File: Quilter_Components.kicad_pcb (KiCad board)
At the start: 4 copper layers, 40.4 x 100 mm, 160 parts, among them J1 Conn_01x10_Male, J2 Conn_01x10_Male, J3 Conn_01x10_Male, J4 Eurorack_10_pin_power, U1 TL072, U10 SSI2144, U2 TL074, U3 TL074, U4 TL074, U5 SSI2144, U7 SSI2144, U9 SSI2144

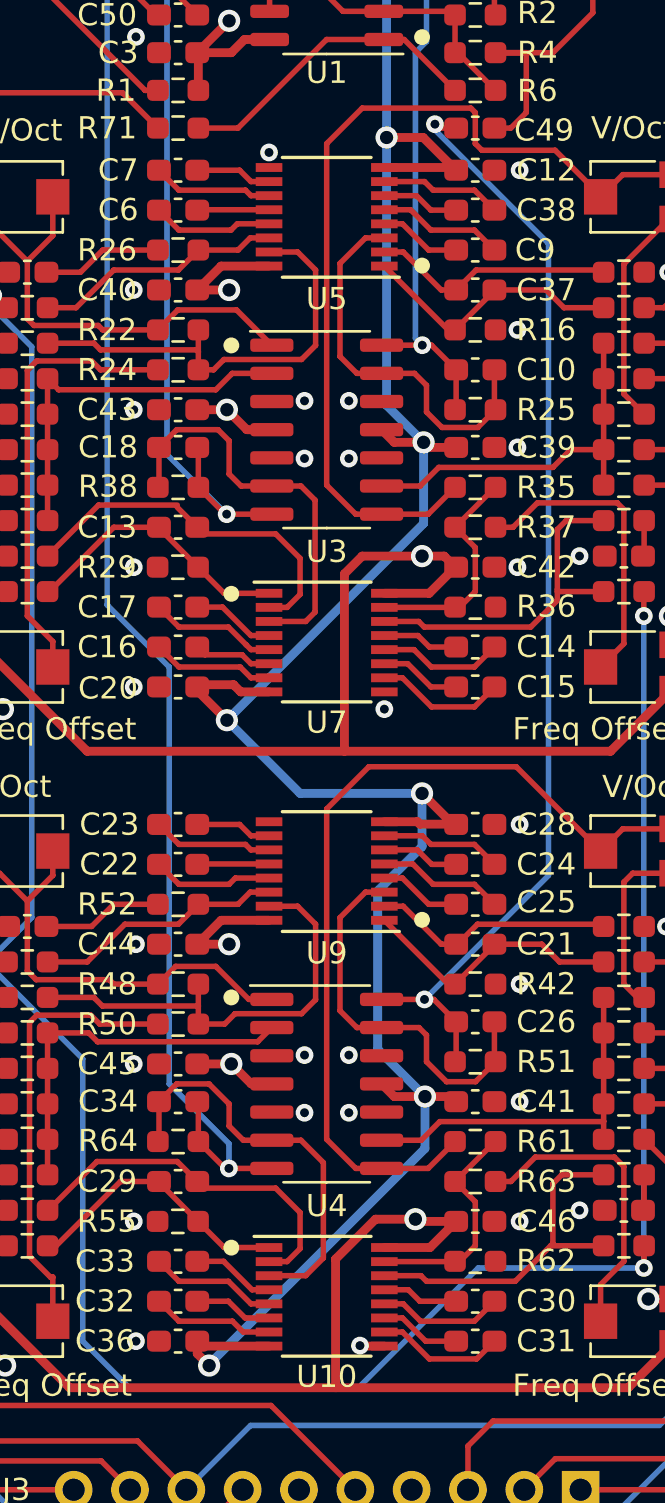
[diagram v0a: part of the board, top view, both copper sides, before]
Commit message: Reorganised components gerber location
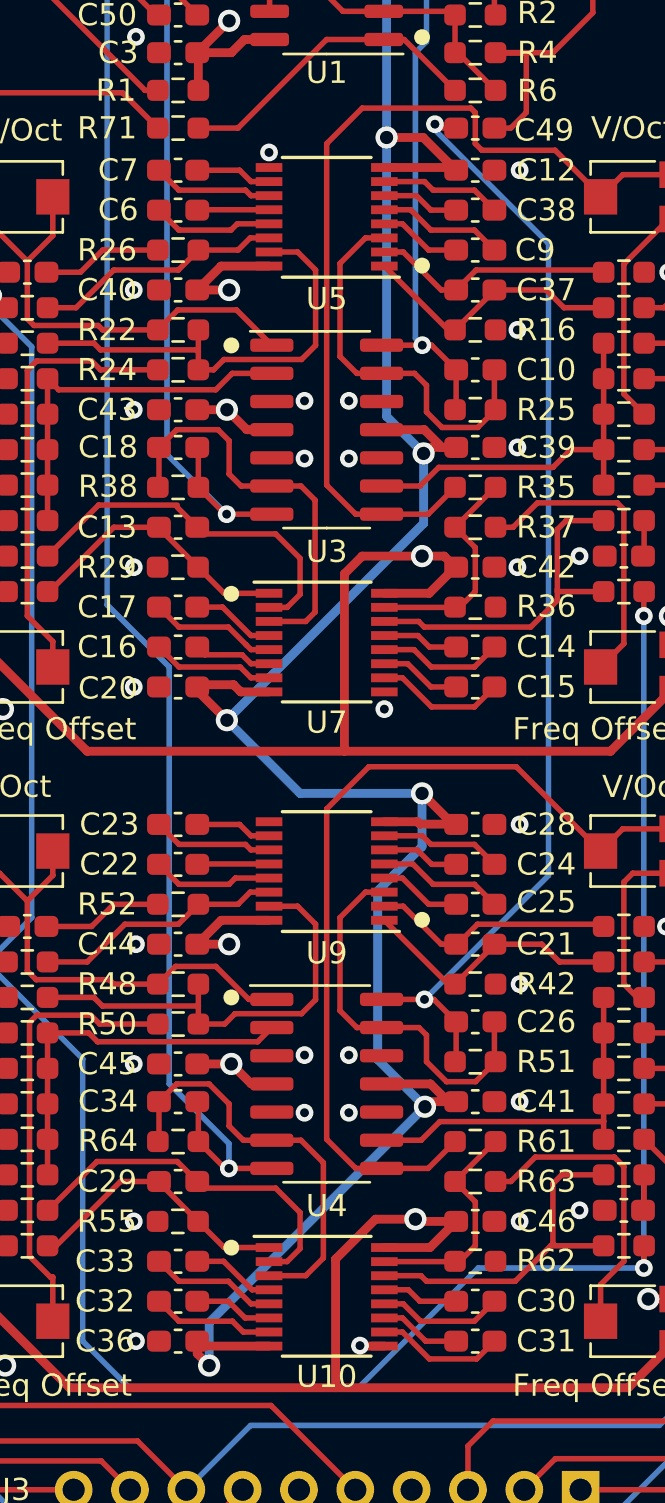
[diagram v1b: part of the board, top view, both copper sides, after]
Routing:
- net -12V: track 226.2 -> 228.5 mm
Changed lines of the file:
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@@
     (pad_to_mask_clearance 0)
     (pcbplotparams
-      (layerselection 0x00010fc_ffffffff)
+      (layerselection 0x00010f0_ffffffff)
       (disableapertmacros false)
       (usegerberextensions false)
@@
       (drillshape 0)
       (scaleselection 1)
-      (outputdirectory "Gerbers/Components/")
+      (outputdirectory "Gerbers/Quilter_Components/")
     )
   )
@@
   (segment (start 64.3625 141.7625) (end 64.9 142.3) (width 0.4) (layer "F.Cu") (net 3))
   (segment (start 66 111.6) (end 64.4625 111.6) (width 0.4) (layer "F.Cu") (net 3))
-  (segment (start 74.57 100.67) (end 73.245 100.67) (width 0.4) (layer "F.Cu") (net 3))
+  (segment (start 74.84 100.9) (end 74.57 101.17) (width 0.4) (layer "F.Cu") (net 3))
   (segment (start 65.2625 70.4) (end 64.3625 69.5) (width 0.4) (layer "F.Cu") (net 3))
   (segment (start 72.775 78.695) (end 72.78 78.7) (width 0.4) (layer "F.Cu") (net 3))
   (segment (start 67.6 111.9225) (end 66.3225 111.9225) (width 0.4) (layer "F.Cu") (net 3))
-  (segment (start 73.245 130.17) (end 72.675 129.6) (width 0.4) (layer "F.Cu") (net 3))
   (segment (start 51.8 56.1) (end 54.3 53.6) (width 0.4) (layer "F.Cu") (net 3))
   (segment (start 64.4125 62.7) (end 63.0125 61.3) (width 0.4) (layer "F.Cu") (net 3))
-  (segment (start 74.8 100.9) (end 74.57 100.67) (width 0.4) (layer "F.Cu") (net 3))
+  (segment (start 75.4 100.9) (end 74.84 100.9) (width 0.4) (layer "F.Cu") (net 3))
   (segment (start 76.0375 88.4) (end 75.915 88.2775) (width 0.4) (layer "F.Cu") (net 3))
   (segment (start 76.0375 117.9) (end 75.9 117.9) (width 0.4) (layer "F.Cu") (net 3))
+  (segment (start 72.675 129.6) (end 74.881374 129.6) (width 0.4) (layer "F.Cu") (net 3))
   (segment (start 72.8 117.7775) (end 74.29 117.7775) (width 0.4) (layer "F.Cu") (net 3))
-  (segment (start 74.63 130.17) (end 73.245 130.17) (width 0.4) (layer "F.Cu") (net 3))
   (segment (start 74.4375 76.4) (end 72.9 76.4) (width 0.4) (layer "F.Cu") (net 3))
   (segment (start 76.0375 88.4) (end 76.026023 88.4) (width 0.4) (layer "F.Cu") (net 3))
+  (segment (start 72.675 100.1) (end 74.6 100.1) (width 0.4) (layer "F.Cu") (net 3))
   (segment (start 58 61.3) (end 56.8 62.5) (width 0.4) (layer "F.Cu") (net 3))
   (segment (start 54.6 111.8) (end 55.5 112.7) (width 0.4) (layer "F.Cu") (net 3))
   (segment (start 85.8 108.6245) (end 85.6755 108.5) (width 0.4) (layer "F.Cu") (net 3))
+  (segment (start 76.0375 130.4) (end 74.86 130.4) (width 0.4) (layer "F.Cu") (net 3))
   (segment (start 74.29 117.7775) (end 74.4 117.8875) (width 0.4) (layer "F.Cu") (net 3))
   (segment (start 55.9 53.8) (end 53.8 55.9) (width 0.4) (layer "F.Cu") (net 3))
   (segment (start 64.585 141.4225) (end 67.6 141.4225) (width 0.4) (layer "F.Cu") (net 3))
+  (segment (start 74.881374 129.6) (end 75.681374 130.4) (width 0.4) (layer "F.Cu") (net 3))
   (segment (start 63.0125 61.3) (end 58 61.3) (width 0.4) (layer "F.Cu") (net 3))
   (segment (start 74.4 117.8875) (end 76.025 117.8875) (width 0.4) (layer "F.Cu") (net 3))
-  (segment (start 76.0375 130.4) (end 75.8075 130.17) (width 0.4) (layer "F.Cu") (net 3))
   (segment (start 54.6 141.3) (end 54.7 141.3) (width 0.4) (layer "F.Cu") (net 3))
-  (segment (start 76.0375 100.9) (end 74.8 100.9) (width 0.4) (layer "F.Cu") (net 3))
   (segment (start 74.550522 86.924499) (end 72.899999 86.924499) (width 0.4) (layer "F.Cu") (net 3))
   (segment (start 53.8 55.9) (end 53.8 59.5) (width 0.4) (layer "F.Cu") (net 3))
@@
   (segment (start 64.585 141.4225) (end 64.3625 141.2) (width 0.4) (layer "F.Cu") (net 3))
   (segment (start 75.9 117.9) (end 74.5 116.5) (width 0.4) (layer "F.Cu") (net 3))
-  (segment (start 75.8075 130.17) (end 74.63 130.17) (width 0.4) (layer "F.Cu") (net 3))
+  (segment (start 75.681374 130.4) (end 76.0375 130.4) (width 0.4) (layer "F.Cu") (net 3))
   (segment (start 75.3375 78.7) (end 76.0375 78) (width 0.4) (layer "F.Cu") (net 3))
   (segment (start 54.7 141.3) (end 55.7 142.3) (width 0.4) (layer "F.Cu") (net 3))
@@
   (segment (start 64.3625 69.5) (end 64.4125 69.55) (width 0.4) (layer "F.Cu") (net 3))
   (segment (start 55.9 53.6) (end 55.9 53.8) (width 0.4) (layer "F.Cu") (net 3))
-  (segment (start 73.245 100.67) (end 72.675 100.1) (width 0.4) (layer "F.Cu") (net 3))
   (segment (start 53.8 59.5) (end 56.8 62.5) (width 0.4) (layer "F.Cu") (net 3))
   (segment (start 64.3625 111.7) (end 64.3625 111.8625) (width 0.4) (layer "F.Cu") (net 3))
@@
   (segment (start 67.725 70.4) (end 65.2625 70.4) (width 0.4) (layer "F.Cu") (net 3))
   (segment (start 64.3625 141.2) (end 64.3625 141.7625) (width 0.4) (layer "F.Cu") (net 3))
+  (segment (start 74.86 130.4) (end 74.63 130.63) (width 0.4) (layer "F.Cu") (net 3))
+  (segment (start 74.6 100.1) (end 75.4 100.9) (width 0.4) (layer "F.Cu") (net 3))
+  (segment (start 76.0375 100.9) (end 75.4 100.9) (width 0.4) (layer "F.Cu") (net 3))
   (segment (start 55.5 112.7) (end 55.6 112.7) (width 0.4) (layer "F.Cu") (net 3))
   (segment (start 72.78 78.7) (end 75.3375 78.7) (width 0.4) (layer "F.Cu") (net 3))
   (via (at 64.9 142.3) (size 1) (drill 0.6) (layers "F.Cu" "B.Cu") (net 3))
   (via (at 72.9 76.4) (size 1) (drill 0.6) (layers "F.Cu" "B.Cu") (net 3))
-  (via (at 74.57 100.67) (size 1) (drill 0.6) (layers "F.Cu" "B.Cu") (net 3))
+  (via (at 74.57 101.17) (size 1) (drill 0.6) (layers "F.Cu" "B.Cu") (net 3))
   (via (at 72.899999 86.924499) (size 1) (drill 0.6) (layers "F.Cu" "B.Cu") (net 3))
   (via (at 84.7 139.3) (size 1) (drill 0.6) (layers "F.Cu" "B.Cu") (net 3))
   (via (at 55.6 112.7) (size 1) (drill 0.6) (layers "F.Cu" "B.Cu") (net 3))
-  (via (at 74.63 130.17) (size 1) (drill 0.6) (layers "F.Cu" "B.Cu") (net 3))
+  (via (at 74.63 130.63) (size 1) (drill 0.6) (layers "F.Cu" "B.Cu") (net 3))
   (via (at 55.7 142.3) (size 1) (drill 0.6) (layers "F.Cu" "B.Cu") (net 3))
   (via (at 65.95 69.55) (size 1) (drill 0.6) (layers "F.Cu" "B.Cu") (net 3))
@@
   (segment (start 56.1 113.2) (end 55.6 112.7) (width 0.4) (layer "In2.Cu") (net 3))
   (segment (start 77.9 116.5) (end 85.7 108.7) (width 0.4) (layer "In2.Cu") (net 3))
-  (segment (start 84.7 139.3) (end 84 139.3) (width 0.4) (layer "In2.Cu") (net 3))
+  (segment (start 75.33 130.63) (end 74.63 130.63) (width 0.4) (layer "In2.Cu") (net 3))
   (segment (start 65.7 113.2) (end 56.1 113.2) (width 0.4) (layer "In2.Cu") (net 3))
   (segment (start 64.845 142.3) (end 55.7 142.3) (width 0.4) (layer "In2.Cu") (net 3))
-  (segment (start 84 139.3) (end 74.87 130.17) (width 0.4) (layer "In2.Cu") (net 3))
-  (segment (start 74.87 130.17) (end 74.63 130.17) (width 0.4) (layer "In2.Cu") (net 3))
-  (segment (start 74.57 100.67) (end 74.57 104.33) (width 0.4) (layer "B.Cu") (net 3))
-  (segment (start 64.9 142.245) (end 64.9 142.3) (width 0.4) (layer "B.Cu") (net 3))
+  (segment (start 84 139.3) (end 75.33 130.63) (width 0.4) (layer "In2.Cu") (net 3))
+  (segment (start 84.7 139.3) (end 84 139.3) (width 0.4) (layer "In2.Cu") (net 3))
+  (segment (start 64.9 140.36) (end 74.63 130.63) (width 0.4) (layer "B.Cu") (net 3))
+  (segment (start 74.5 118.9) (end 72.5 120.9) (width 0.4) (layer "B.Cu") (net 3))
   (segment (start 65.95 69.55) (end 72.8 76.4) (width 0.4) (layer "B.Cu") (net 3))
-  (segment (start 72.9 99) (end 72.899999 86.924499) (width 0.4) (layer "B.Cu") (net 3))
+  (segment (start 72.899999 86.924499) (end 72.899999 99.499999) (width 0.4) (layer "B.Cu") (net 3))
   (segment (start 72.899999 86.924499) (end 72.9 76.4) (width 0.4) (layer "B.Cu") (net 3))
-  (segment (start 74.63 132.515) (end 64.9 142.245) (width 0.4) (layer "B.Cu") (net 3))
+  (segment (start 72.899999 99.499999) (end 74.57 101.17) (width 0.4) (layer "B.Cu") (net 3))
   (segment (start 56.8 62.5) (end 63.85 69.55) (width 0.4) (layer "B.Cu") (net 3))
-  (segment (start 74.63 130.17) (end 72.5 128.04) (width 0.4) (layer "B.Cu") (net 3))
-  (segment (start 74.63 130.17) (end 74.63 132.515) (width 0.4) (layer "B.Cu") (net 3))
-  (segment (start 72.5 120.9) (end 74.5 118.9) (width 0.4) (layer "B.Cu") (net 3))
-  (segment (start 74.57 100.67) (end 72.9 99) (width 0.4) (layer "B.Cu") (net 3))
-  (segment (start 72.5 128.04) (end 72.5 120.9) (width 0.4) (layer "B.Cu") (net 3))
-  (segment (start 74.57 104.33) (end 65.7 113.2) (width 0.4) (layer "B.Cu") (net 3))
+  (segment (start 74.57 104.33) (end 74.57 101.17) (width 0.4) (layer "B.Cu") (net 3))
+  (segment (start 72.5 128.5) (end 74.63 130.63) (width 0.4) (layer "B.Cu") (net 3))
+  (segment (start 65.7 113.2) (end 74.57 104.33) (width 0.4) (layer "B.Cu") (net 3))
   (segment (start 69 116.5) (end 74.5 116.5) (width 0.4) (layer "B.Cu") (net 3))
-  (segment (start 74.5 118.9) (end 74.5 116.5) (width 0.4) (layer "B.Cu") (net 3))
+  (segment (start 74.5 116.5) (end 74.5 118.9) (width 0.4) (layer "B.Cu") (net 3))
+  (segment (start 64.9 142.3) (end 64.9 140.36) (width 0.4) (layer "B.Cu") (net 3))
   (segment (start 65.7 113.2) (end 69 116.5) (width 0.4) (layer "B.Cu") (net 3))
+  (segment (start 72.5 120.9) (end 72.5 128.5) (width 0.4) (layer "B.Cu") (net 3))
   (segment (start 72.8 76.4) (end 72.9 76.4) (width 0.4) (layer "B.Cu") (net 3))
   (segment (start 63.85 69.55) (end 65.95 69.55) (width 0.4) (layer "B.Cu") (net 3))
